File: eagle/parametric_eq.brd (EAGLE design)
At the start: 100 x 80 mm, 41 parts, among them IC1 TL072P, IC2 TL072P

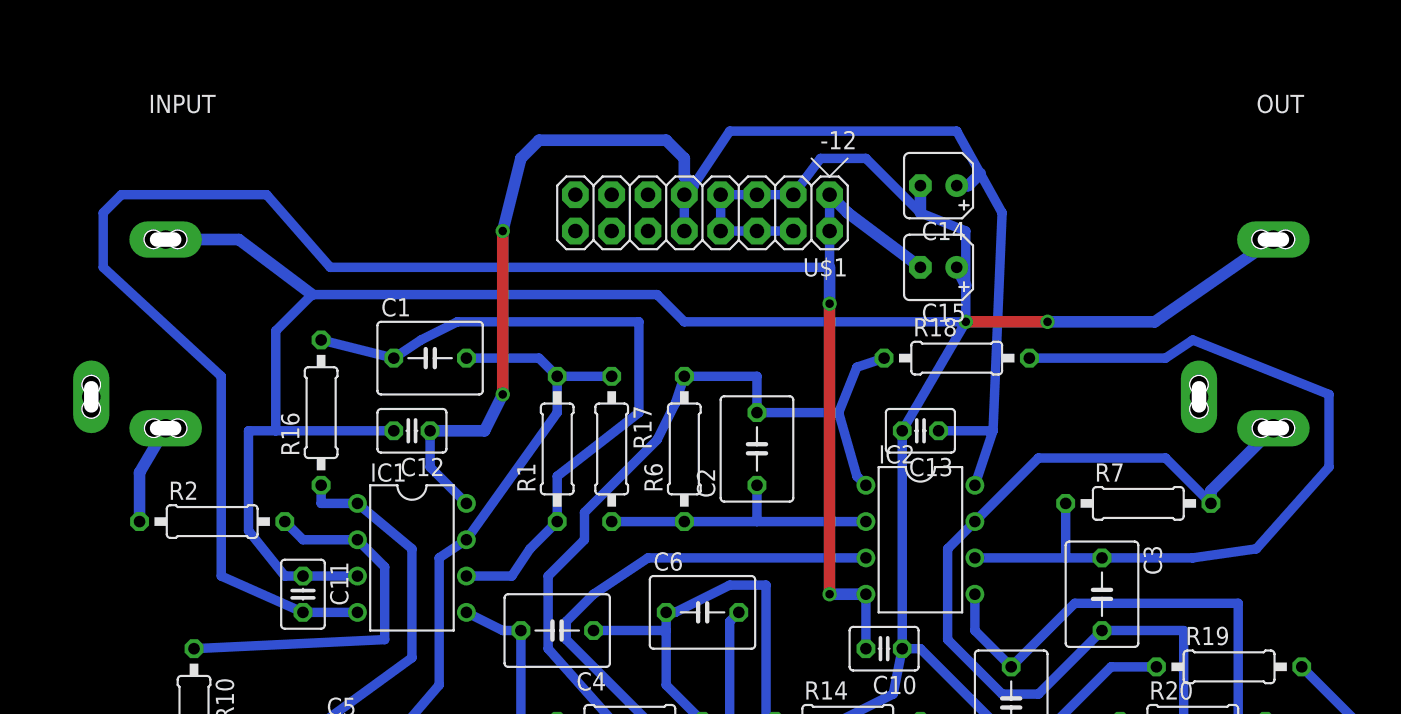
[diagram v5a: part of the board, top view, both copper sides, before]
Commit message: dc reject cap
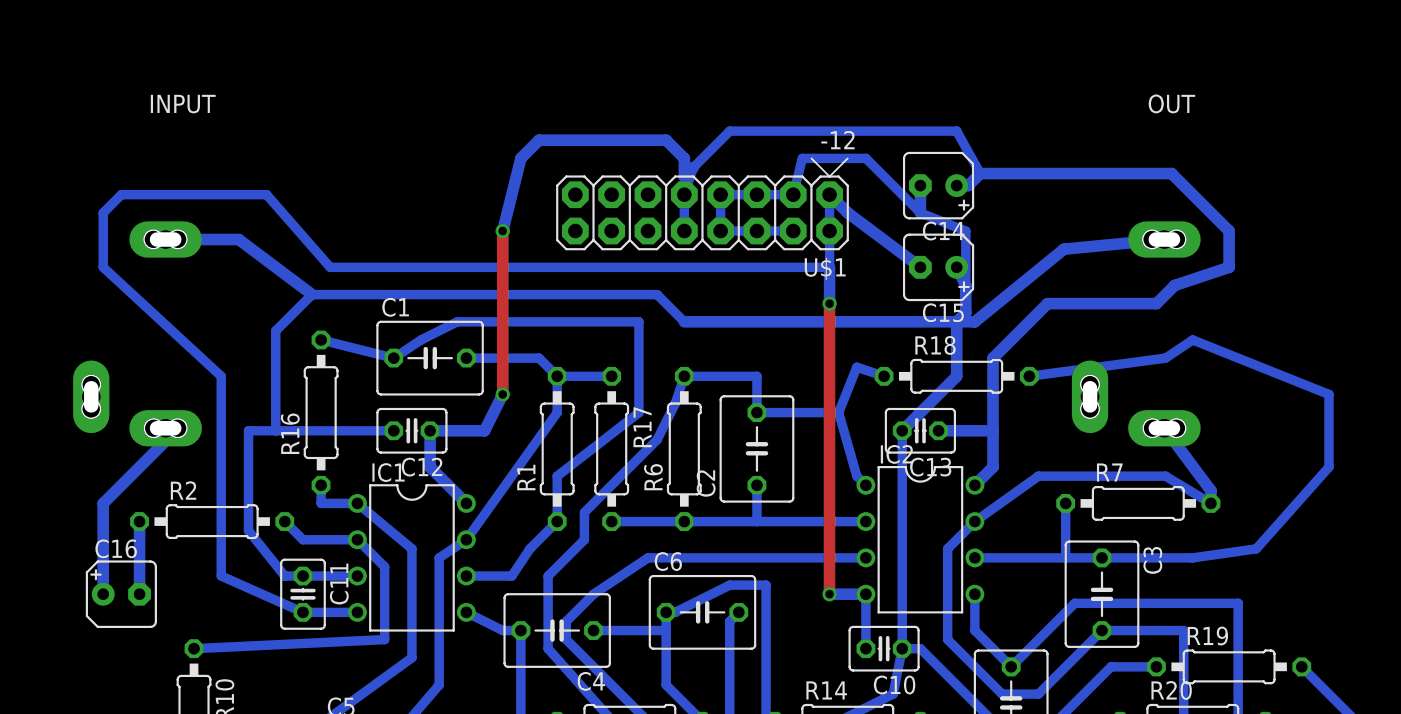
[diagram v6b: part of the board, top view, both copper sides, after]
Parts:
- added C16: 10u, rcl:B45181A
- moved OUT 7.62 mm to (76.8, 55.2)
- moved R18 1.27 mm to (67.3, 43.2)
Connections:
- new net N$24: C16.-, R2.1
- net N$9: now also C16.+; no longer R2.1
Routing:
- net +12V: track 99.6 -> 127.2 mm
- net N$9: track 7.02 -> 13.4 mm
- net GND: track 245.6 -> 239.4 mm, vias 2 -> 0
- net N$24: track 0.00 -> 5.08 mm
- net N$8: track 76.3 -> 74.0 mm
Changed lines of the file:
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@@
 <element name="IC1" library="linear" package="DIL08" value="TL072P" x="29.21" y="30.48" rot="R270"/>
 <element name="IC2" library="linear" package="DIL08" value="TL072P" x="64.77" y="31.75" rot="R270"/>
-<element name="OUT" library="erthenvar" package="ERTHENVAR-JACK-90DEG" value="AUDIO-JACK" x="84.455" y="55.245"/>
+<element name="OUT" library="erthenvar" package="ERTHENVAR-JACK-90DEG" value="AUDIO-JACK" x="76.835" y="55.245"/>
 <element name="INPUT" library="erthenvar" package="ERTHENVAR-JACK-90DEG" value="AUDIO-JACK" x="6.985" y="55.245"/>
 <element name="R1" library="rcl" package="0207/10" value="2k2" x="39.37" y="38.1" rot="R90"/>
@@
 <element name="R16" library="rcl" package="0207/10" value="2k2" x="22.86" y="40.64" rot="R90"/>
 <element name="R17" library="rcl" package="0207/10" value="2k2" x="43.18" y="38.1" rot="R270"/>
-<element name="R18" library="rcl" package="0207/10" value="2k2" x="67.31" y="44.45"/>
+<element name="R18" library="rcl" package="0207/10" value="2k2" x="67.31" y="43.18"/>
 <element name="R19" library="rcl" package="0207/10" value="4k7" x="86.36" y="22.86"/>
 <element name="R2" library="rcl" package="0207/10" value="2k" x="15.24" y="33.02"/>
@@
 <element name="C14" library="rcl" package="B45181A" value="10u" x="66.04" y="56.515" rot="R180"/>
 <element name="C15" library="rcl" package="B45181A" value="10u" x="66.04" y="50.8" rot="R180"/>
+<element name="C16" library="rcl" package="B45181A" value="10u" x="8.89" y="27.94"/>
 </elements>
 <signals>
@@
 <wire x1="77.47" y1="30.48" x2="74.93" y2="30.48" width="0.6604" layer="16"/>
 <wire x1="74.93" y1="30.48" x2="68.58" y2="30.48" width="0.6604" layer="16"/>
-<wire x1="81.915" y1="44.45" x2="72.39" y2="44.45" width="0.6604" layer="16"/>
+<wire x1="81.915" y1="44.45" x2="72.39" y2="43.18" width="0.6604" layer="16"/>
 <wire x1="83.82" y1="45.72" x2="81.915" y2="44.45" width="0.6604" layer="16"/>
 <wire x1="93.345" y1="41.91" x2="83.82" y2="45.72" width="0.6604" layer="16"/>
@@
 <wire x1="60.325" y1="43.815" x2="59.055" y2="40.64" width="0.6604" layer="16"/>
 <wire x1="59.055" y1="40.64" x2="60.325" y2="36.195" width="0.6604" layer="16"/>
-<wire x1="62.23" y1="44.45" x2="60.325" y2="43.815" width="0.6604" layer="16"/>
+<wire x1="62.23" y1="43.18" x2="60.325" y2="43.815" width="0.6604" layer="16"/>
 <wire x1="53.34" y1="43.18" x2="48.26" y2="43.18" width="0.6604" layer="16"/>
 <wire x1="53.34" y1="40.64" x2="53.34" y2="43.18" width="0.6604" layer="16"/>
@@
 <contactref element="OUT" pad="P$3"/>
 <contactref element="HILEV" pad="3"/>
-<wire x1="73.025" y1="37.465" x2="68.58" y2="33.02" width="0.6604" layer="16"/>
-<wire x1="81.915" y1="37.465" x2="73.025" y2="37.465" width="0.6604" layer="16"/>
-<wire x1="85.09" y1="34.29" x2="81.915" y2="37.465" width="0.6604" layer="16"/>
+<wire x1="73.025" y1="36.195" x2="68.58" y2="33.02" width="0.6604" layer="16"/>
+<wire x1="81.915" y1="36.195" x2="73.025" y2="36.195" width="0.6604" layer="16"/>
+<wire x1="85.09" y1="34.29" x2="81.915" y2="36.195" width="0.6604" layer="16"/>
 <wire x1="83.185" y1="25.4" x2="77.47" y2="25.4" width="0.6604" layer="16"/>
 <wire x1="83.185" y1="5.715" x2="83.185" y2="25.4" width="0.6604" layer="16"/>
@@
 <wire x1="77.47" y1="25.4" x2="73.025" y2="20.955" width="0.6604" layer="16"/>
 <wire x1="85.09" y1="34.29" x2="85.09" y2="35.18" width="0.8128" layer="16"/>
-<wire x1="85.09" y1="35.18" x2="89.455" y2="39.545" width="0.8128" layer="16"/>
+<wire x1="85.09" y1="35.18" x2="81.835" y2="39.545" width="0.8128" layer="16"/>
 </signal>
 <signal name="N$10">
@@
 <contactref element="U$1" pad="10"/>
 <wire x1="48.26" y1="55.88" x2="48.26" y2="53.34" width="0.6604" layer="16"/>
-<wire x1="69.85" y1="39.37" x2="66.04" y2="39.37" width="0.6604" layer="16"/>
-<wire x1="51.435" y1="60.325" x2="48.895" y2="56.515" width="0.6604" layer="16"/>
-<wire x1="48.895" y1="56.515" x2="48.26" y2="55.88" width="0.6604" layer="16"/>
-<wire x1="70.485" y1="54.61" x2="68.95740625" y2="57.35966875" width="0.6604" layer="16"/>
+<wire x1="51.435" y1="60.325" x2="48.895" y2="57.785" width="0.6604" layer="16"/>
+<wire x1="48.895" y1="57.785" x2="48.26" y2="55.88" width="0.6604" layer="16"/>
 <wire x1="68.95740625" y1="57.35966875" x2="67.31" y2="60.325" width="0.6604" layer="16"/>
 <wire x1="67.31" y1="60.325" x2="51.435" y2="60.325" width="0.6604" layer="16"/>
-<wire x1="68.58" y1="35.56" x2="69.85" y2="39.37" width="0.6604" layer="16"/>
-<wire x1="69.85" y1="39.37" x2="70.485" y2="54.61" width="0.6604" layer="16"/>
-<wire x1="30.48" y1="36.83" x2="33.02" y2="34.29" width="0.6604" layer="16"/>
-<wire x1="30.48" y1="39.37" x2="30.48" y2="36.83" width="0.6604" layer="16"/>
 <wire x1="30.48" y1="39.37" x2="34.29" y2="39.37" width="0.8128" layer="16"/>
 <wire x1="34.29" y1="39.37" x2="35.56" y2="41.91" width="0.8128" layer="16"/>
@@
 <wire x1="46.99" y1="59.69" x2="48.26" y2="58.42" width="0.8128" layer="16"/>
 <wire x1="48.26" y1="58.42" x2="48.26" y2="57.15" width="0.8128" layer="16"/>
-<wire x1="48.26" y1="57.15" x2="48.895" y2="56.515" width="0.8128" layer="16"/>
+<wire x1="48.26" y1="57.15" x2="48.895" y2="57.785" width="0.8128" layer="16"/>
 <contactref element="C14" pad="+"/>
 <wire x1="67.31" y1="56.515" x2="68.1127375" y2="56.515" width="0.8128" layer="16"/>
 <wire x1="68.1127375" y1="56.515" x2="68.95740625" y2="57.35966875" width="0.8128" layer="16"/>
+<wire x1="68.95740625" y1="57.35966875" x2="82.34033125" y2="57.35966875" width="0.8128" layer="16"/>
+<wire x1="82.34033125" y1="57.35966875" x2="86.36" y2="53.34" width="0.8128" layer="16"/>
+<wire x1="86.36" y1="53.34" x2="86.36" y2="50.8" width="0.8128" layer="16"/>
+<wire x1="86.36" y1="50.8" x2="82.55" y2="49.53" width="0.8128" layer="16"/>
+<wire x1="82.55" y1="49.53" x2="81.28" y2="48.26" width="0.8128" layer="16"/>
+<wire x1="81.28" y1="48.26" x2="73.66" y2="48.26" width="0.8128" layer="16"/>
+<wire x1="73.66" y1="48.26" x2="69.85" y2="44.45" width="0.8128" layer="16"/>
+<wire x1="69.85" y1="44.45" x2="69.85" y2="39.37" width="0.8128" layer="16"/>
+<wire x1="66.04" y1="39.37" x2="69.85" y2="39.37" width="0.8128" layer="16"/>
+<wire x1="69.85" y1="39.37" x2="69.85" y2="36.83" width="0.8128" layer="16"/>
+<wire x1="69.85" y1="36.83" x2="68.58" y2="35.56" width="0.8128" layer="16"/>
+<wire x1="30.48" y1="36.83" x2="33.02" y2="34.29" width="0.8128" layer="16"/>
+<wire x1="30.48" y1="36.83" x2="30.48" y2="39.37" width="0.8128" layer="16"/>
 </signal>
 <signal name="-12V">
@@
 <wire x1="71.12" y1="17.78" x2="73.025" y2="17.78" width="0.6604" layer="16"/>
 <wire x1="63.5" y1="24.13" x2="63.5" y2="39.37" width="0.6604" layer="16"/>
-<wire x1="57.785" y1="58.42" x2="55.88" y2="55.88" width="0.6604" layer="16"/>
+<wire x1="56.515" y1="58.42" x2="55.88" y2="55.88" width="0.6604" layer="16"/>
 <wire x1="67.945" y1="53.34" x2="64.77" y2="54.61" width="0.6604" layer="16"/>
 <wire x1="64.77" y1="54.61" x2="60.96" y2="58.42" width="0.6604" layer="16"/>
-<wire x1="60.96" y1="58.42" x2="57.785" y2="58.42" width="0.6604" layer="16"/>
-<wire x1="63.5" y1="39.37" x2="67.945" y2="46.99" width="0.6604" layer="16"/>
-<wire x1="67.945" y1="46.99" x2="67.945" y2="49.53" width="0.6604" layer="16"/>
+<wire x1="60.96" y1="58.42" x2="56.515" y2="58.42" width="0.6604" layer="16"/>
 <wire x1="67.945" y1="49.53" x2="67.945" y2="53.34" width="0.6604" layer="16"/>
 <wire x1="47.625" y1="26.67" x2="46.99" y2="26.67" width="0.6604" layer="16"/>
@@
 <wire x1="19.685" y1="46.355" x2="19.685" y2="39.37" width="0.6604" layer="16"/>
 <wire x1="22.225" y1="48.895" x2="19.685" y2="46.355" width="0.6604" layer="16"/>
-<wire x1="67.945" y1="46.99" x2="48.26" y2="46.99" width="0.6604" layer="16"/>
 <wire x1="48.26" y1="46.99" x2="46.355" y2="48.895" width="0.6604" layer="16"/>
 <wire x1="46.355" y1="48.895" x2="22.225" y2="48.895" width="0.6604" layer="16"/>
-<via x="67.945" y="46.99" extent="1-16" drill="0.6" shape="square"/>
-<wire x1="67.945" y1="46.99" x2="73.66" y2="46.99" width="0.8128" layer="1"/>
-<via x="73.66" y="46.99" extent="1-16" drill="0.6" shape="square"/>
-<wire x1="73.66" y1="46.99" x2="81.16" y2="46.99" width="0.8128" layer="16"/>
-<wire x1="81.16" y1="46.99" x2="89.455" y2="52.745" width="0.8128" layer="16"/>
+<wire x1="68.58" y1="46.99" x2="74.81" y2="52.07" width="0.8128" layer="16"/>
+<wire x1="74.81" y1="52.07" x2="81.835" y2="52.745" width="0.8128" layer="16"/>
 <wire x1="11.985" y1="52.745" x2="17.105" y2="52.745" width="0.8128" layer="16"/>
 <wire x1="17.105" y1="52.745" x2="22.225" y2="48.895" width="0.8128" layer="16"/>
@@
 <wire x1="67.31" y1="50.8" x2="67.945" y2="49.53" width="0.8128" layer="16"/>
 <wire x1="64.77" y1="56.515" x2="64.77" y2="54.61" width="0.8128" layer="16"/>
+<wire x1="48.26" y1="46.99" x2="67.31" y2="46.99" width="0.8128" layer="16"/>
+<wire x1="67.31" y1="46.99" x2="68.58" y2="46.99" width="0.8128" layer="16"/>
+<wire x1="67.945" y1="49.53" x2="67.945" y2="47.625" width="0.8128" layer="16"/>
+<wire x1="67.945" y1="47.625" x2="67.31" y2="46.99" width="0.8128" layer="16"/>
+<wire x1="67.31" y1="46.99" x2="67.31" y2="43.18" width="0.8128" layer="16"/>
+<wire x1="67.31" y1="43.18" x2="63.5" y2="39.37" width="0.8128" layer="16"/>
 </signal>
 <signal name="N$22">
@@
 </signal>
 <signal name="N$9">
+<contactref element="INPUT" pad="P$3"/>
+<contactref element="C16" pad="+"/>
+<wire x1="11.985" y1="39.545" x2="11.985" y2="38.655" width="0.8128" layer="16"/>
+<wire x1="11.985" y1="38.655" x2="7.62" y2="34.29" width="0.8128" layer="16"/>
+<wire x1="7.62" y1="34.29" x2="7.62" y2="27.94" width="0.8128" layer="16"/>
+</signal>
+<signal name="N$24">
+<contactref element="C16" pad="-"/>
 <contactref element="R2" pad="1"/>
-<contactref element="INPUT" pad="P$3"/>
-<wire x1="10.16" y1="33.02" x2="10.16" y2="36.45" width="0.8128" layer="16"/>
-<wire x1="10.16" y1="36.45" x2="11.985" y2="39.545" width="0.8128" layer="16"/>
+<wire x1="10.16" y1="27.94" x2="10.16" y2="33.02" width="0.8128" layer="16"/>
 </signal>
 </signals>

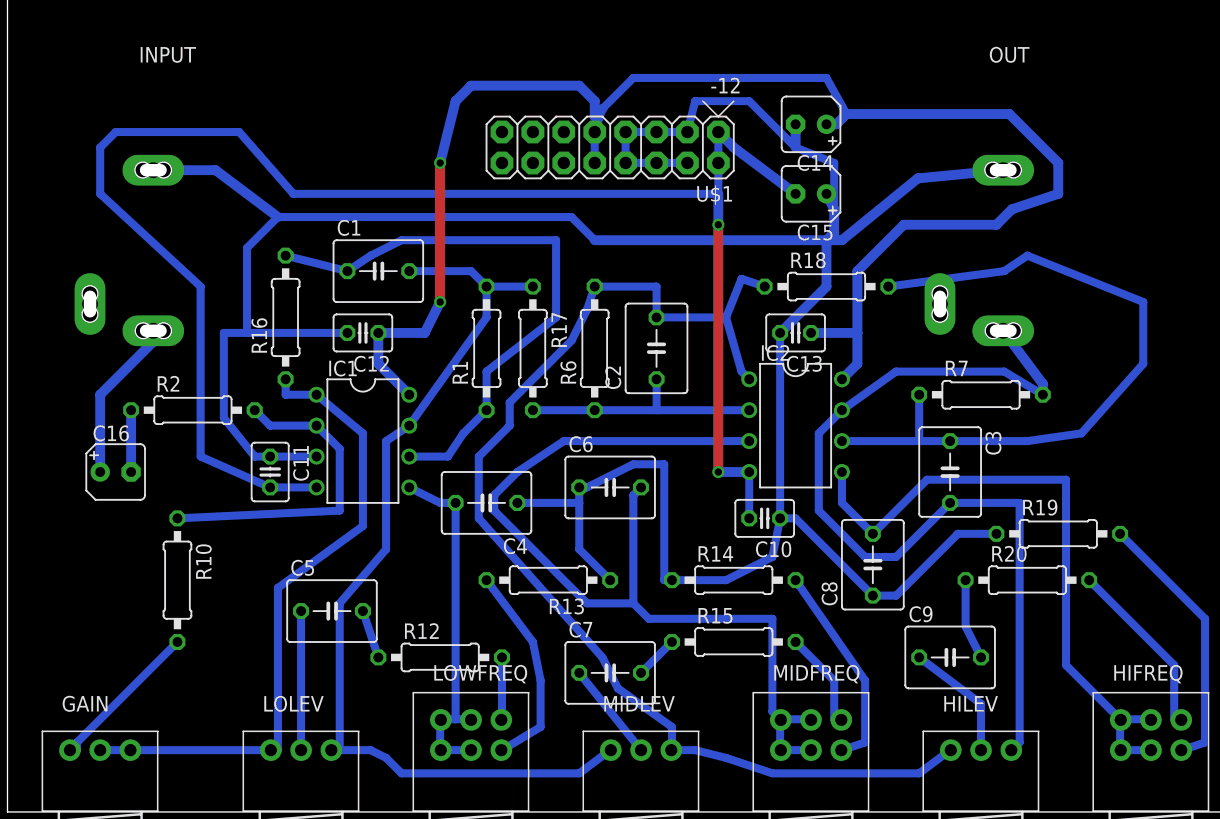
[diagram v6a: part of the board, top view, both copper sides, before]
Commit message: improved traces
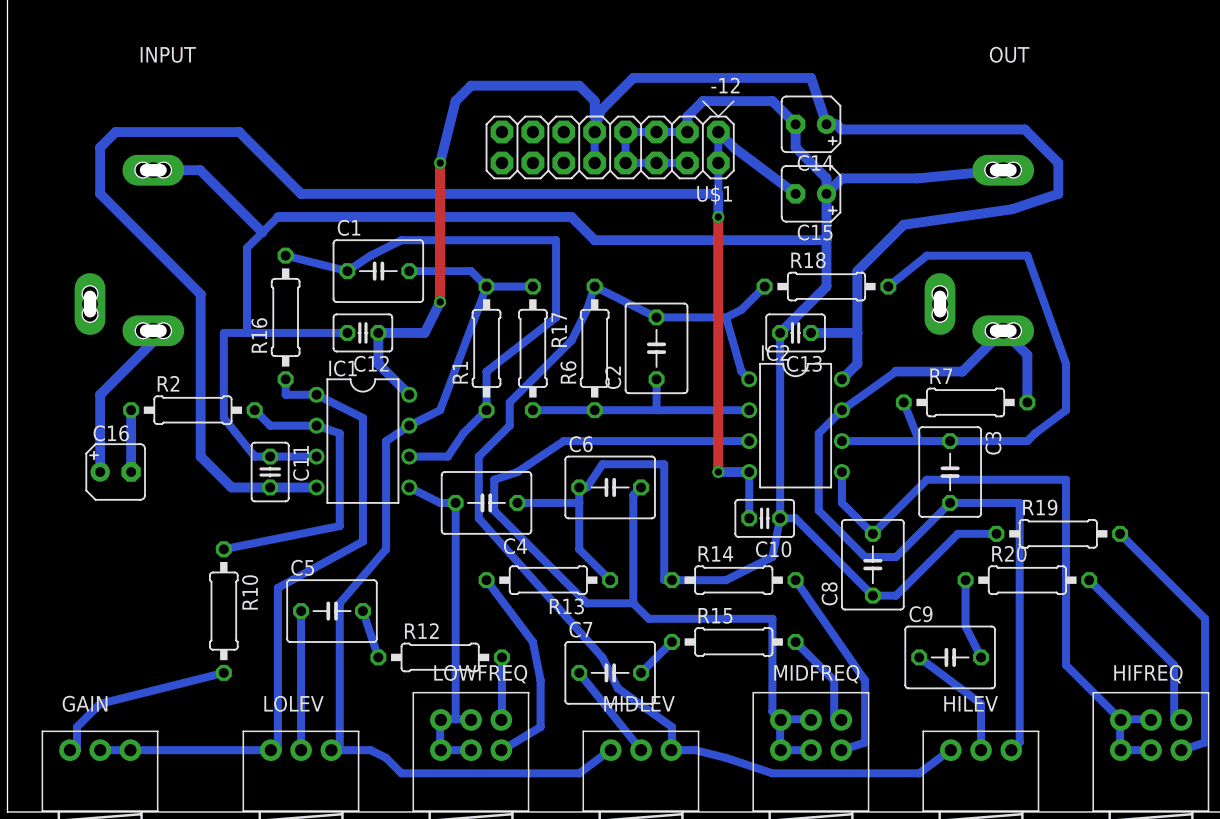
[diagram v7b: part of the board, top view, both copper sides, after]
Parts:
- moved R10 4.58 mm to (17.8, 16.5)
- moved R7 1.42 mm to (78.7, 33.7)
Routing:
- net N$4: track 58.4 -> 48.3 mm
- net GND: track 239.4 -> 234.5 mm
- net N$7: track 96.3 -> 93.0 mm
- net N$2: track 12.9 -> 15.7 mm
- net N$8: track 74.0 -> 72.0 mm
- net N$1: track 26.7 -> 24.9 mm
- net +12V: track 127.2 -> 125.4 mm
- net N$23: track 53.0 -> 54.1 mm
- net N$27: track 76.3 -> 76.9 mm
